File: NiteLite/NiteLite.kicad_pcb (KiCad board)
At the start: 2 copper layers, 77.4 x 24.5 mm, 15 parts, among them J1 USB_B_Micro, J2 USB_A, U1 7555, U2 TLV1117-33, X1 Badgelife_sao_connector_v169b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

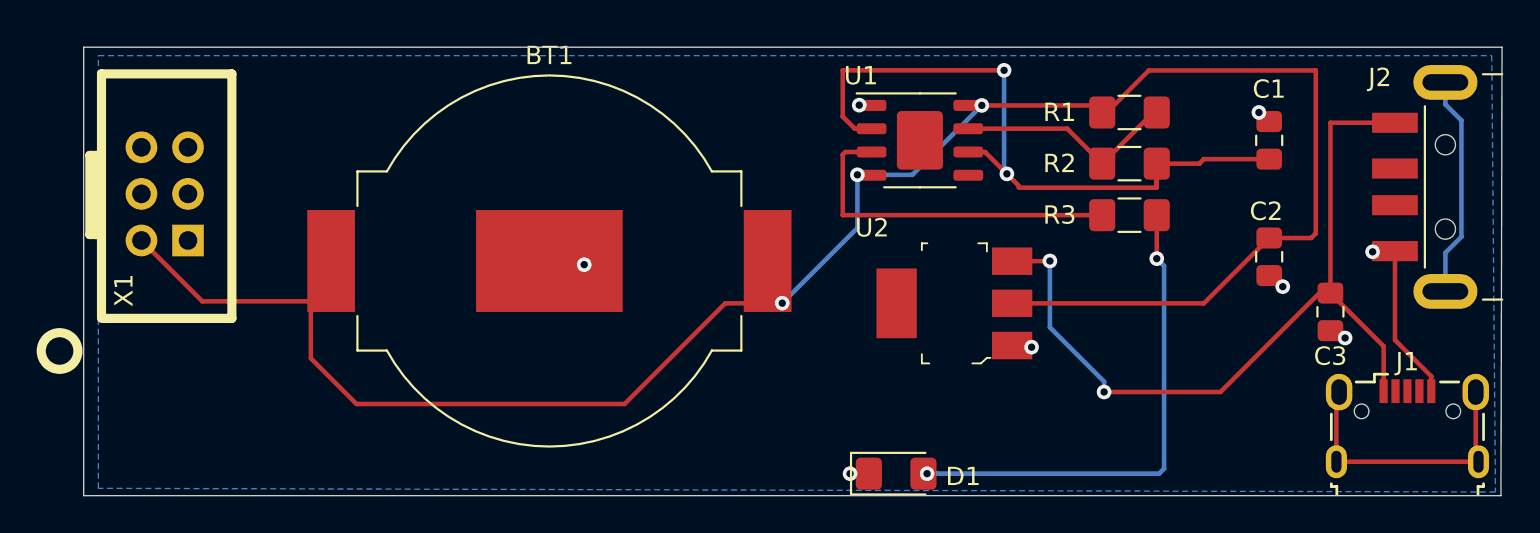
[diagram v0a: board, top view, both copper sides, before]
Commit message: updates to artwork and sch
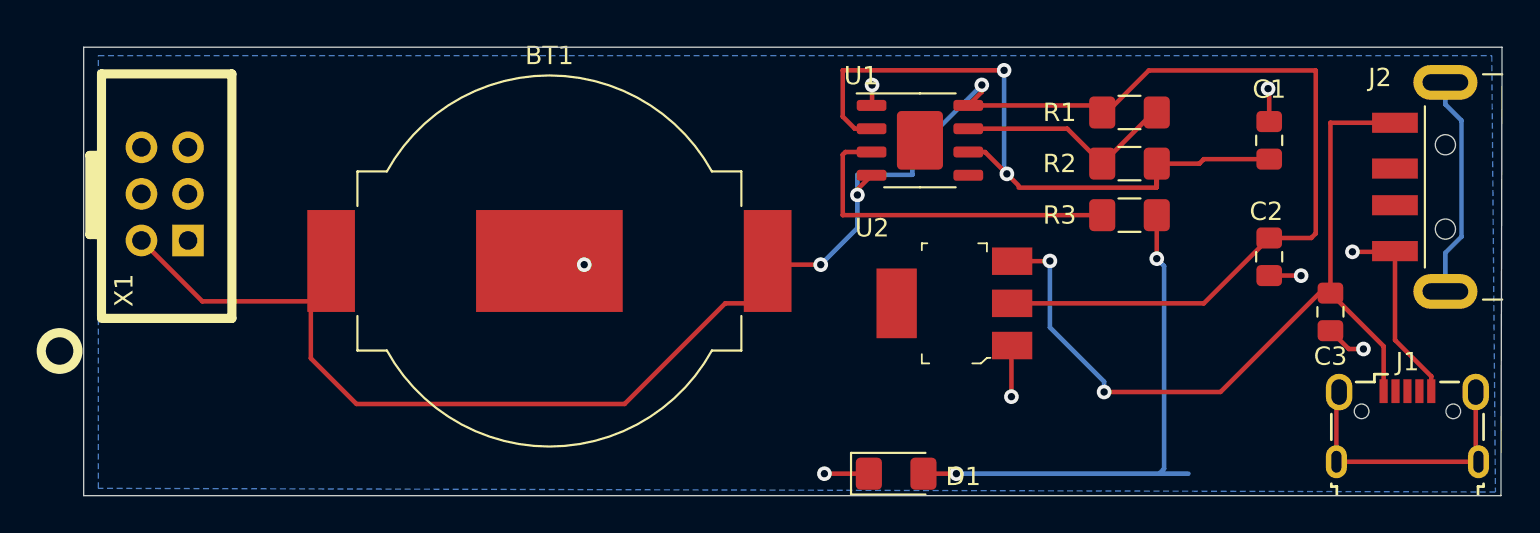
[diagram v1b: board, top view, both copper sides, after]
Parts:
- removed the G*** at (141.2, 116.8)
- added G***: LOGO, New:test60x60, B.Cu at (89.6, 124.8)
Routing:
- net GND: track 14.2 -> 26.4 mm
- net Net-(BT1-Pad1): track 106.9 -> 110.8 mm
- net Net-(D1-Pad2): track 27.9 -> 29.1 mm
